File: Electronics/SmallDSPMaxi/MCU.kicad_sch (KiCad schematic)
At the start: 47 parts, among them J21 Header, J22 Header, J23 Header, J24 Header, Q2 2N7002, Q3 2N7002, Q4 2N7002, SW3 TS-1187A-B-A-B, U14 STM32F030C8Tx, Y2 8MHz

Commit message: Fixes minor issues
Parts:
- removed R62, R63, R64, R65, R66, R68, R69, R71, R72: 100k, Resistor_SMD:R_0402_1005Metric, symbol Device:R_Small
- added R3 (x9): 10k, Resistor_SMD:R_0402_1005Metric, symbol Device:R_Small
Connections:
- net +3V3: now also R3.1, R3.1, R3.1, R3.1, R3.1, R3.1, R3.1, R3.1, R3.1
- net ~{CS Codec 1}: now also R3.2
- net ~{CS Codec 2}: now also R3.2
- net ~{CS Codec 3}: now also R3.2
- net ~{CS Codec 4}: now also R3.2
- net ~{CS Codec 5}: now also R3.2
- net ~{CS Codec 6}: now also R3.2
- net ~{CS Codec 7}: now also R3.2
- net ~{CS Codec 8}: now also R3.2
- net ~{RST}: now also R3.2

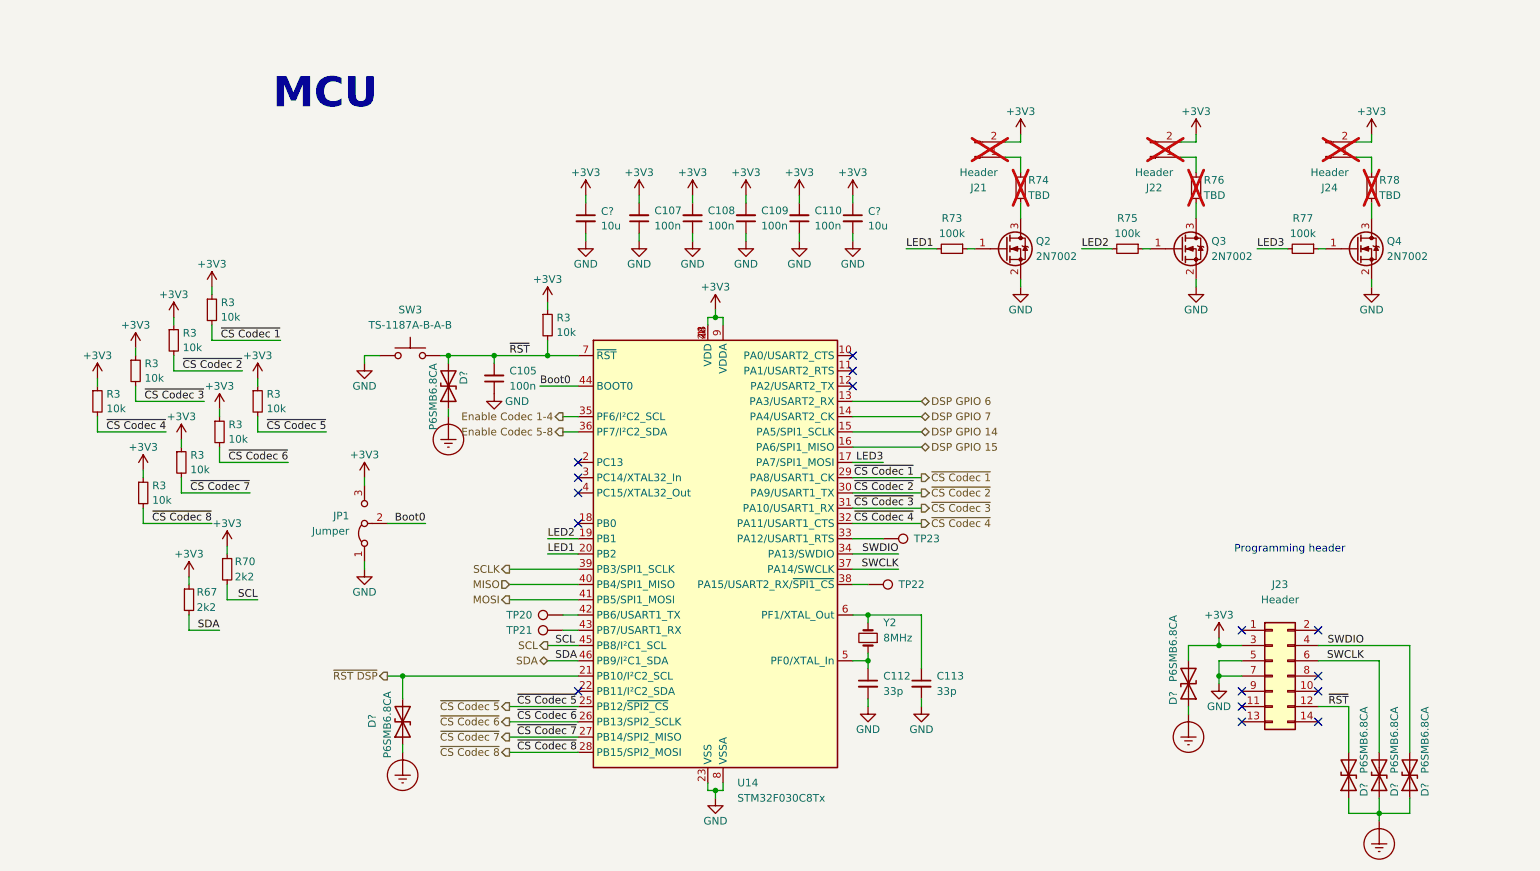
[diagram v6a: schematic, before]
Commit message: adds usb to i2s bridge to micro. Adds tweaks for layout of maxi.
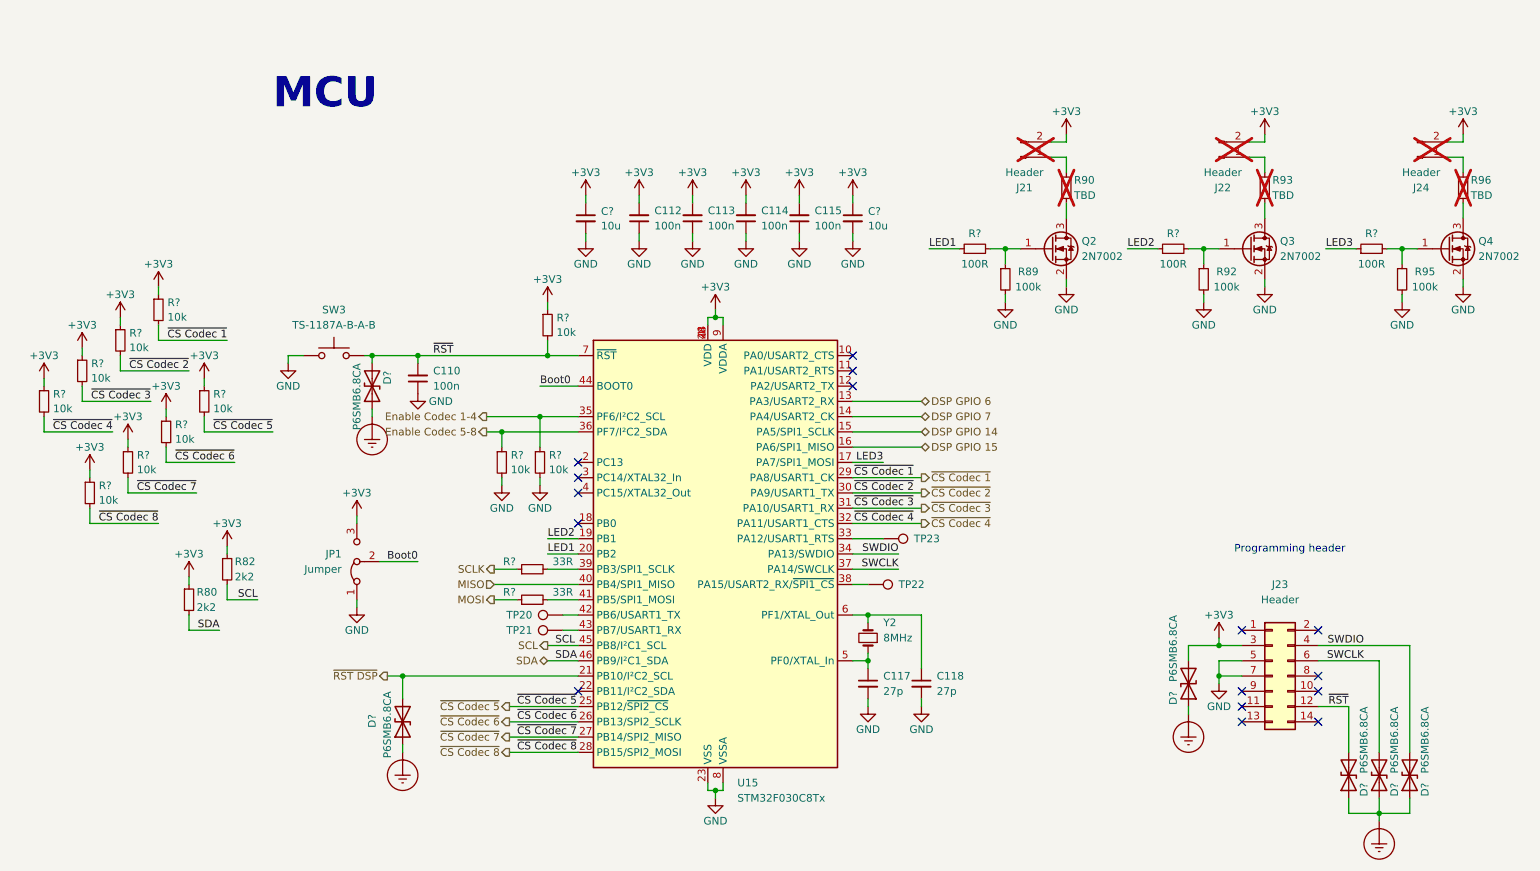
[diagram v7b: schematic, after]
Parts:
- added R? (x2): 33R, Resistor_SMD:R_0402_1005Metric, symbol Device:R_Small
- added R? (x3): 100R, Resistor_SMD:R_0402_1005Metric, symbol Device:R_Small
- added R? (x2): 10k, Resistor_SMD:R_0402_1005Metric, symbol Device:R_Small
- C117: renamed from C112; value 33p -> 27p; LCSC Part # C1562 -> C1557; Part Number 0402CG330J500NT -> 0402CG270J500NT
- C118: renamed from C113; value 33p -> 27p; LCSC Part # C1562 -> C1557; Part Number 0402CG330J500NT -> 0402CG270J500NT
- renumbered C105 to C110, C107 to C112, C108 to C113, C109 to C114, C110 to C115, R67 to R80, R70 to R82, R73 to R89, R74 to R90, R75 to R92, R76 to R93, R77 to R95, R78 to R96, R3 to R?, U14 to U15
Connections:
- net Enable Codec 1-4: now also R?.1
- net Enable Codec 5-8: now also R?.1
- net GND: now also R89.2, R92.2, R95.2, R?.2, R?.2
- net LED1: now also R?.1; no longer R89.2
- net LED2: now also R?.1; no longer R92.2
- net LED3: now also R?.1; no longer R95.2
- net MOSI: now also R?.1; no longer U15.41 (PB5/SPI1_MOSI)
- net SCLK: now also R?.1; no longer U15.39 (PB3/SPI1_SCLK)
- net at Q2.1 (G), R89.1: now also R?.2
- net at Q3.1 (G), R92.1: now also R?.2
- net at Q4.1 (G), R95.1: now also R?.2
- new net: R?.2, U15.41 (PB5/SPI1_MOSI)
- new net: R?.2, U15.39 (PB3/SPI1_SCLK)
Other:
- moved on the sheet: C110, D?, J21, J22, J24, JP1, Q2, Q3, Q4, R89, R90, R92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

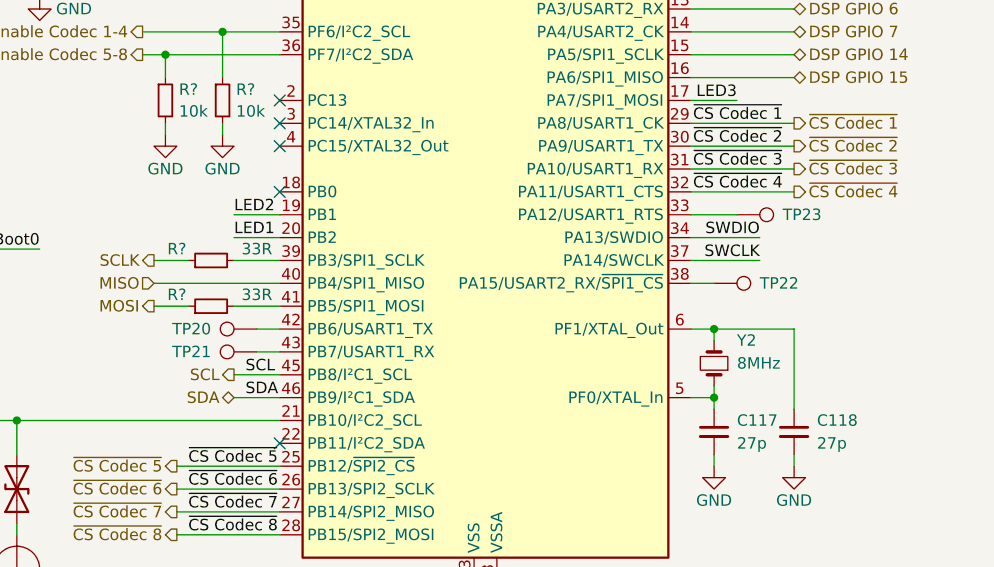
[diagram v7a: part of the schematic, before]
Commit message: Fixes wrong connection in maxi schematic
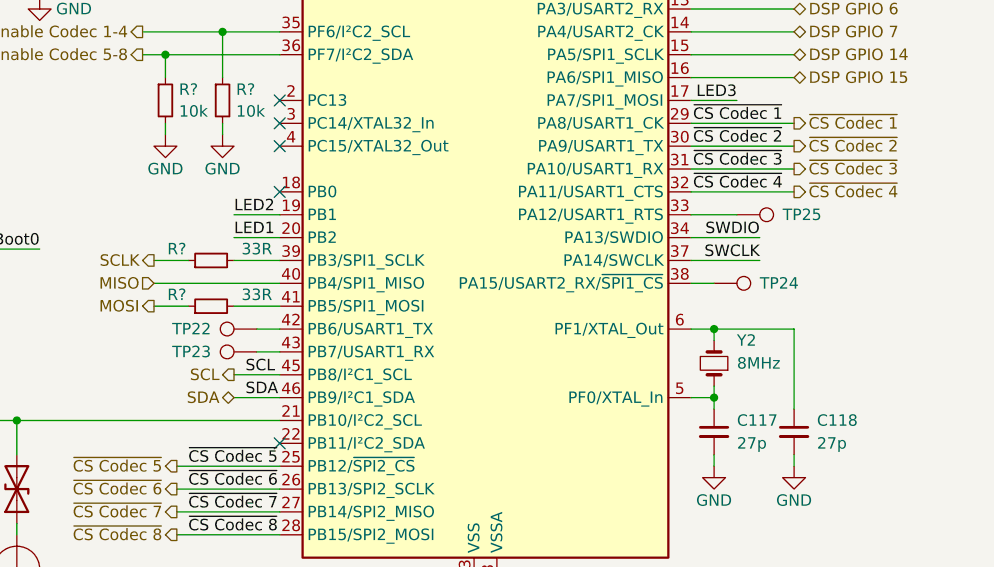
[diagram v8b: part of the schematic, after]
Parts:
- renumbered TP20 to TP22, TP21 to TP23, TP22 to TP24, TP23 to TP25
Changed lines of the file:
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@@
   (title_block
     (title "SmallDSP Maxi")
-    (date "2023-11-10")
+    (date "2023-12-01")
     (rev "1.0")
     (company "Till Heuer")
@@
   (symbol (lib_id "Connector:TestPoint") (at 105.41 116.84 90) (unit 1)
     (in_bom yes) (on_board yes) (dnp no)
-    (property "Reference" "TP21" (at 100.33 116.84 90)
+    (property "Reference" "TP23" (at 100.33 116.84 90)
       (effects (font (size 1.27 1.27)) (justify left))
     )
@@
       (project "SmallDSPMaxi"
         (path "/5f2729b5-edcd-4fbc-b3fb-44096724c941/d67cb9b8-3550-4a9a-a119-4a7c3ea5cb86"
-          (reference "TP21") (unit 1)
+          (reference "TP23") (unit 1)
         )
       )
@@
   (symbol (lib_id "Connector:TestPoint") (at 156.21 109.22 270) (unit 1)
     (in_bom yes) (on_board yes) (dnp no)
-    (property "Reference" "TP22" (at 161.29 109.22 90)
+    (property "Reference" "TP24" (at 161.29 109.22 90)
       (effects (font (size 1.27 1.27)) (justify left))
     )
@@
       (project "SmallDSPMaxi"
         (path "/5f2729b5-edcd-4fbc-b3fb-44096724c941/d67cb9b8-3550-4a9a-a119-4a7c3ea5cb86"
-          (reference "TP22") (unit 1)
+          (reference "TP24") (unit 1)
         )
       )
@@
   (symbol (lib_id "Connector:TestPoint") (at 158.75 101.6 270) (unit 1)
     (in_bom yes) (on_board yes) (dnp no)
-    (property "Reference" "TP23" (at 163.83 101.6 90)
+    (property "Reference" "TP25" (at 163.83 101.6 90)
       (effects (font (size 1.27 1.27)) (justify left))
     )
@@
       (project "SmallDSPMaxi"
         (path "/5f2729b5-edcd-4fbc-b3fb-44096724c941/d67cb9b8-3550-4a9a-a119-4a7c3ea5cb86"
-          (reference "TP23") (unit 1)
+          (reference "TP25") (unit 1)
         )
       )
@@
   (symbol (lib_id "Connector:TestPoint") (at 105.41 114.3 90) (unit 1)
     (in_bom yes) (on_board yes) (dnp no)
-    (property "Reference" "TP20" (at 100.33 114.3 90)
+    (property "Reference" "TP22" (at 100.33 114.3 90)
       (effects (font (size 1.27 1.27)) (justify left))
     )
@@
       (project "SmallDSPMaxi"
         (path "/5f2729b5-edcd-4fbc-b3fb-44096724c941/d67cb9b8-3550-4a9a-a119-4a7c3ea5cb86"
-          (reference "TP20") (unit 1)
+          (reference "TP22") (unit 1)
         )
       )
